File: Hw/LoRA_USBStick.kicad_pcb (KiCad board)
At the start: 2 copper layers, 61.5 x 18.7 mm, 18 parts, among them J10 USB_B, J4 SWD, SW1 RST, U1 ATSAMD21E, U2 RFM95W-868S2, U3 AP2112K-3.3

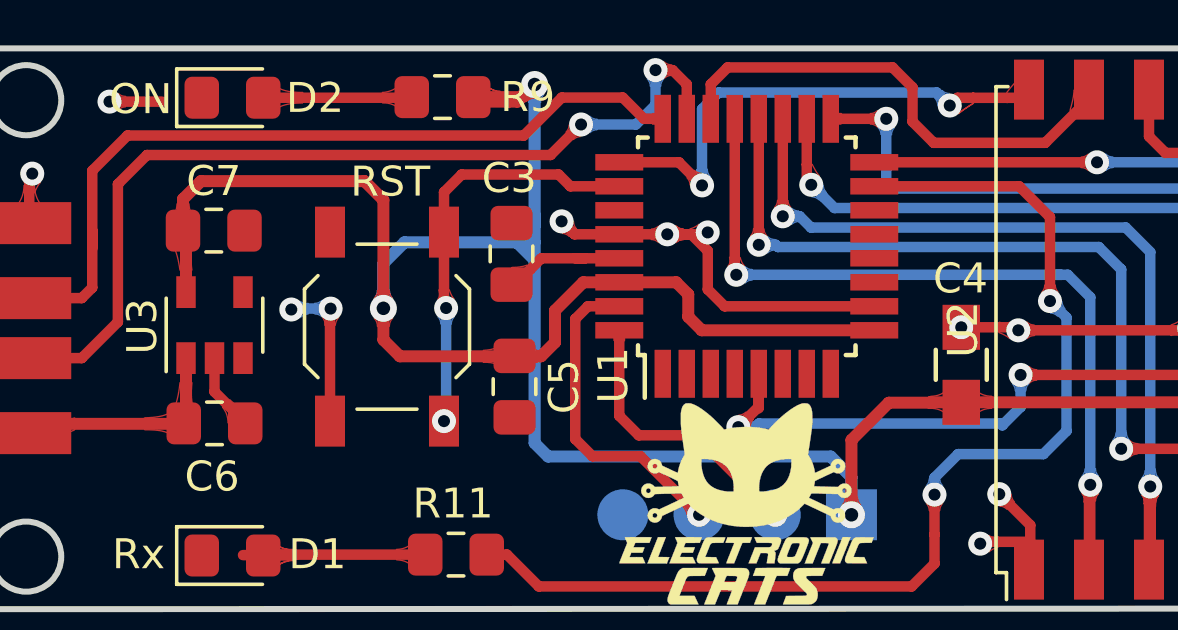
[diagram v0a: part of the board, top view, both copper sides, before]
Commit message: Fix layout on enable LDO
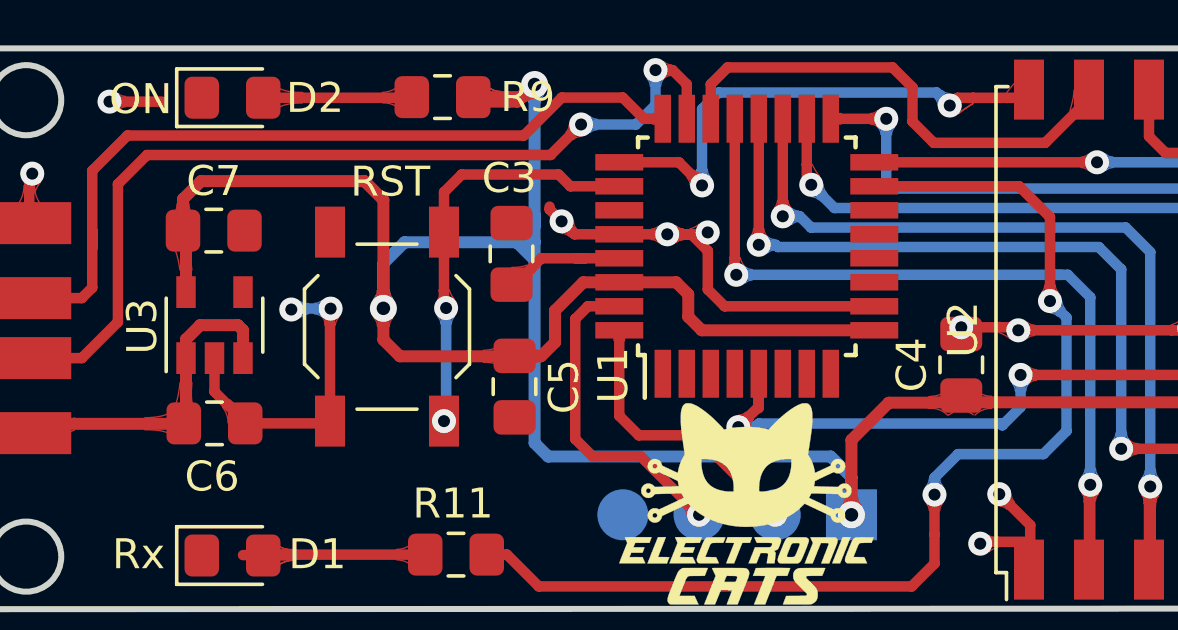
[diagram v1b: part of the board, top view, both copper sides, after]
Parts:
- C4: footprint Capacitors_SMD:C_0805_HandSoldering -> Capacitor_SMD:C_0805_2012Metric_Pad1.15x1.40mm_HandSolder
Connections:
- U3 pad 3: Net-(U3-Pad3) -> VBUS
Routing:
- net VBUS: track 6.92 -> 10.6 mm
- net GND: track 57.1 -> 60.6 mm

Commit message: Change labels, assigned and check the footprints
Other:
- net class Default removed
- net class Vcc+ removed
- net class vcc removed

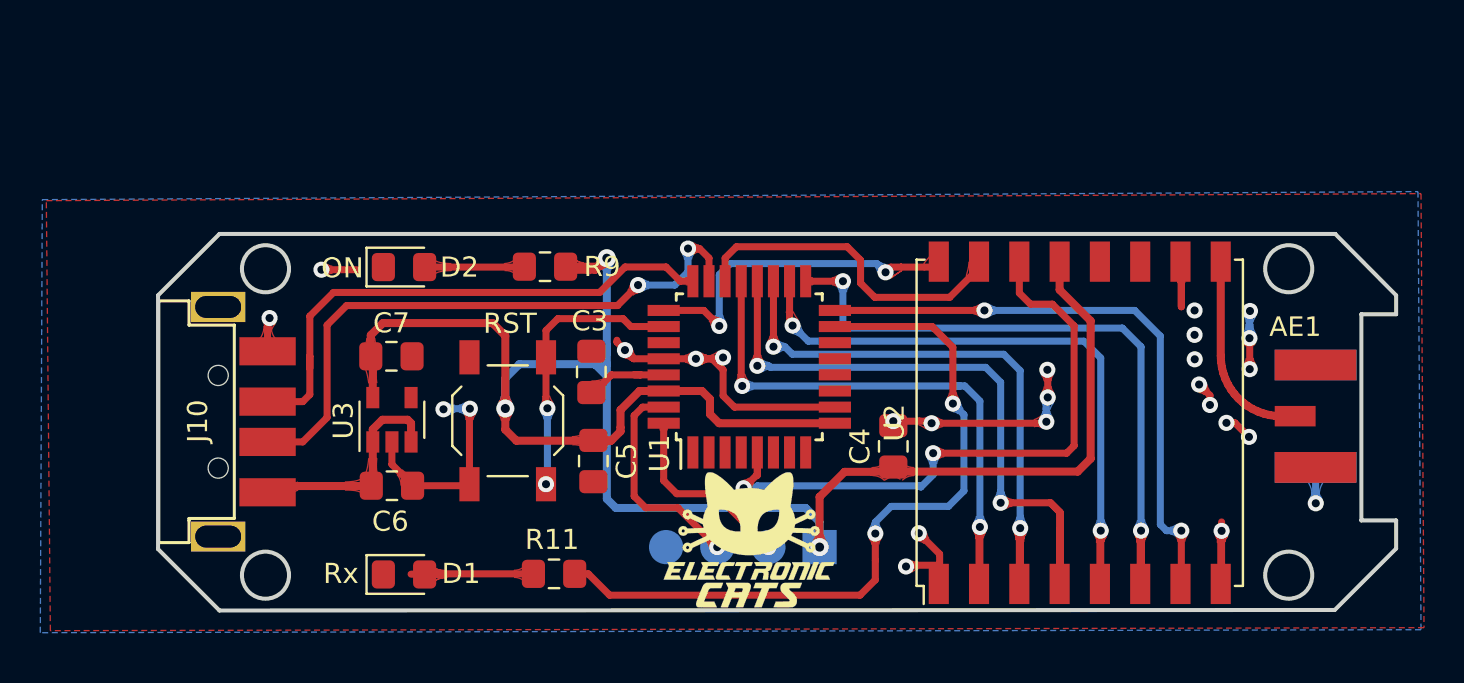
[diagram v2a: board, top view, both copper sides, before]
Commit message: Place footprints on the PCB
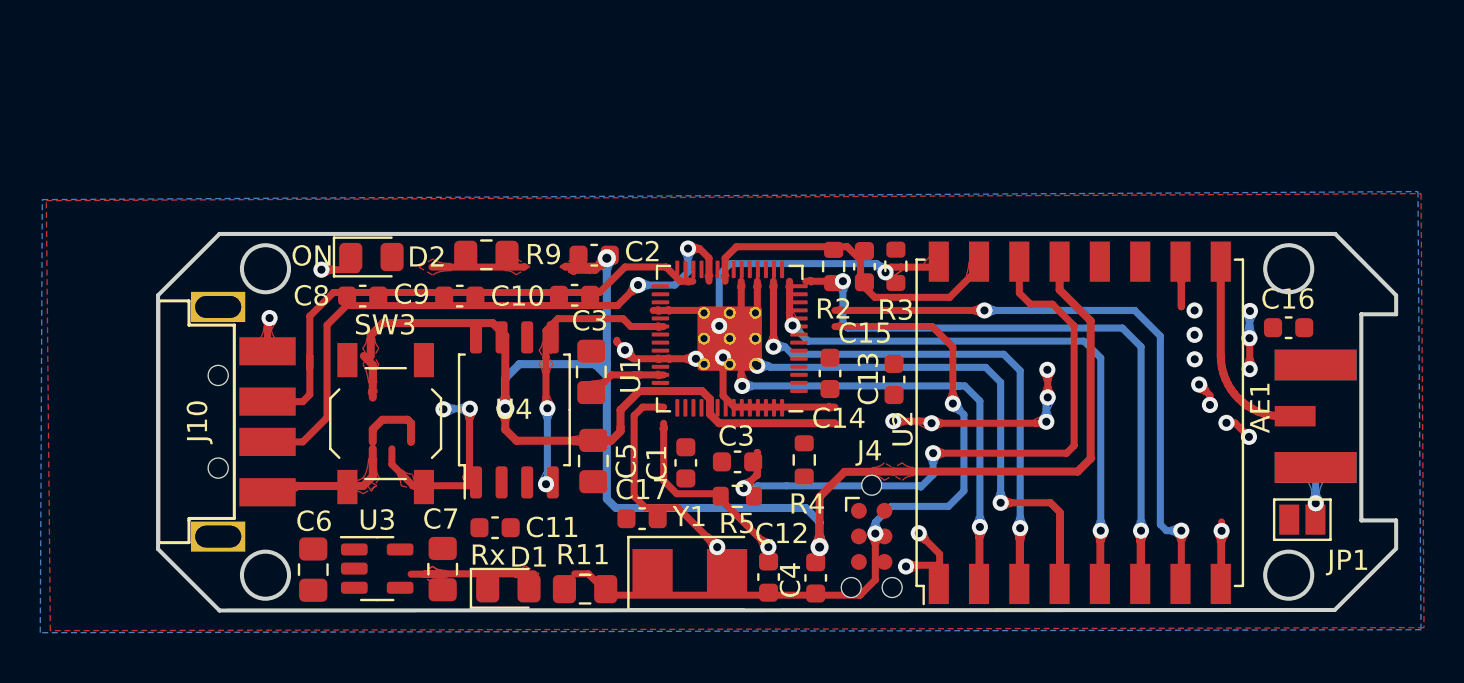
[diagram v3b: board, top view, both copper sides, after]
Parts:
- removed the G*** at (146.1, 120.0)
- removed SW1: RST, Button_Switch_SMD:SW_SPST_TL3342
- added C1: 27pF, Capacitor_SMD:C_0603_1608Metric, F.Cu at (143.0, 116.1)
- added C10: 0.1uF, Capacitor_SMD:C_0603_1608Metric, F.Cu at (137.5, 107.8)
- added C11: 0.1uF, Capacitor_SMD:C_0603_1608Metric, F.Cu at (133.5, 119.4)
- added C12: 0.1uF, Capacitor_SMD:C_0603_1608Metric, F.Cu at (147.1, 121.8)
- added C13: 0.1uF, Capacitor_SMD:C_0603_1608Metric, F.Cu at (153.3, 112.0)
- added C14: 0.1uF, Capacitor_SMD:C_0603_1608Metric, F.Cu at (150.2, 111.7)
- added C15: 0.1uF, Capacitor_SMD:C_0603_1608Metric, F.Cu at (151.9, 106.4)
- added C16: 0.1uF, Capacitor_SMD:C_0603_1608Metric, F.Cu at (172.9, 109.4)
- added C17: 0.1uF, Capacitor_SMD:C_0603_1608Metric, F.Cu at (140.8, 118.9)
- added C2: 1uF, Capacitor_SMD:C_0603_1608Metric, F.Cu at (138.4, 105.8)
- added C3: 27pF, Capacitor_SMD:C_0603_1608Metric, F.Cu at (145.6, 116.1)
- added C8: 0.1uF, Capacitor_SMD:C_0603_1608Metric, F.Cu at (127.0, 107.9)
- added C9: 1uF, Capacitor_SMD:C_0603_1608Metric, F.Cu at (131.8, 107.9)
- added JP1: BOOT, Jumper:SolderJumper-2_P1.3mm_Open_Pad1.0x1.5mm, F.Cu at (173.6, 119.0)
- added R2: 1K, Resistor_SMD:R_0603_1608Metric, F.Cu at (150.3, 106.4)
- added R3: 27, Resistor_SMD:R_0603_1608Metric, F.Cu at (153.4, 106.4)
- added R4: 27, Resistor_SMD:R_0603_1608Metric, F.Cu at (148.9, 116.0)
- added R5: 10K, Resistor_SMD:R_0603_1608Metric, F.Cu at (145.6, 117.8)
- added SW3: RST, Button_Switch_SMD:SW_SPST_TL3342, F.Cu at (128.1, 114.2)
- added U4: W25Q16JV, Package_SO:SOIC-8_5.275x5.275mm_P1.27mm, F.Cu at (134.5, 113.5)
- added Y1: 12Mhz, Crystal:Crystal_SMD_5032-2Pin_5.0x3.2mm, F.Cu at (143.2, 121.6)
- C4: footprint Capacitor_SMD:C_0805_2012Metric_Pad1.15x1.40mm_HandSolder -> Capacitor_SMD:C_0603_1608Metric
- J4: footprint Pin_Headers:Pin_Header_Straight_1x04_Pitch2.54mm -> Connector:Tag-Connect_TC2030-IDC-NL_2x03_P1.27mm_Vertical; moved to F.Cu
- U1: value ATSAMD21E -> RP2040; footprint Housings_QFP:TQFP-32_7x7mm_Pitch0.8mm -> RP2040:RP2040-QFN-56
- moved C7 10.9 mm to (130.9, 121.4), turned to -90 degrees
- moved C4 7.58 mm to (149.4, 121.8), turned to -90 degrees
- moved U3 7.43 mm to (127.7, 121.4), turned to 0 degrees
- moved C6 5.71 mm to (124.5, 121.4), turned to -90 degrees
- moved D1 5.23 mm to (134.2, 122.4)
- moved R9 2.97 mm to (133.1, 105.8)
- moved J4 2.64 mm to (152.2, 119.8), turned to -90 degrees
- moved R11 1.72 mm to (138.0, 122.4)
- moved U1 1.71 mm to (145.2, 110.0), turned to 180 degrees
- moved D2 1.69 mm to (127.4, 105.9)
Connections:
- net Net-(U1-Pad2) renamed /RX_LED
- C4 pad 1: +3V3 -> +1V2
- J4 pad 3: /SWCLK -> /RST
- J4 pad 4: GND -> /SWCLK
- U1 pad 1: Net-(U1-Pad1) -> +3V3
- U1 pad 10: GND -> +3V3
- U1 pad 11: Net-(U1-Pad11) -> unconnected-(U1-Pad11)
- U1 pad 12: Net-(U1-Pad12) -> unconnected-(U1-Pad12)
- U1 pad 13: Net-(U1-Pad13) -> /DIO0
- U1 pad 14: Net-(U1-Pad14) -> /DIO1
- U1 pad 15: /Rx_LED -> /DIO2
- U1 pad 16: /DIO5 -> unconnected-(U1-Pad16)
- U1 pad 17: /RFM_RST -> unconnected-(U1-Pad17)
- U1 pad 18: /SS -> /DIO5
- U1 pad 19: /MOSI -> GND
- U1 pad 20: /SCK -> Net-(C1-Pad1)
- U1 pad 21: /MISO -> Net-(R2-Pad2)
- U1 pad 22: /DIO1 -> +3V3
- U1 pad 23: /D- -> +1V2
- U1 pad 24: /D+ -> /SWCLK
- U1 pad 25: /DIO2 -> /SWDIO
- U1 pad 27: Net-(U1-Pad27) -> /MISO
- U1 pad 28: GND -> /SS
- U1 pad 29: Net-(C3-Pad1) -> /SCK
- U1 pad 3: Net-(U1-Pad3) -> unconnected-(U1-Pad3)
- U1 pad 30: +3V3 -> /MOSI
- U1 pad 31: /SWCLK -> unconnected-(U1-Pad31)
- U1 pad 32: /SWDIO -> /RFM_RST
- U1 pad 4: Net-(U1-Pad4) -> unconnected-(U1-Pad4)
- U1 pad 5: /DIO0 -> unconnected-(U1-Pad5)
- U1 pad 6: Net-(U1-Pad6) -> unconnected-(U1-Pad6)
- U1 pad 7: Net-(U1-Pad7) -> unconnected-(U1-Pad7)
- U1 pad 8: Net-(U1-Pad8) -> unconnected-(U1-Pad8)
- U1 pad 9: +3V3 -> unconnected-(U1-Pad9)
- U2 pad 11: Net-(U2-Pad11) -> unconnected-(U2-Pad11)
- U2 pad 12: Net-(U2-Pad12) -> unconnected-(U2-Pad12)
- U3 pad 4: Net-(U3-Pad4) -> unconnected-(U3-Pad4)
- U3 pad 5: +3V3 -> unconnected-(U3-Pad5)
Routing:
- net GND: track 60.6 -> 248.2 mm, vias 26 -> 31
- net /Rx_LED: track 37.2 -> 0.00 mm, vias 2 -> 0
- net /SS: track 31.4 -> 66.0 mm, vias 2 -> 4
- net /RFM_RST: track 34.6 -> 0.00 mm, vias 2 -> 0
- net /SCK: track 34.5 -> 0.00 mm, vias 2 -> 0
- net Net-(C3-Pad1): track 4.50 -> 36.6 mm, vias 0 -> 2
- net /DIO0: track 32.1 -> 0.00 mm, vias 2 -> 0
- net unconnected-(U1-Pad16): track 0.00 -> 30.5 mm, vias 0 -> 2
- net /MOSI: track 30.5 -> 0.00 mm, vias 2 -> 0
- net /MISO: track 28.6 -> 0.00 mm, vias 2 -> 0
- net /D+: track 28.3 -> 0.00 mm
- net /QSPI_CS: track 0.00 -> 21.4 mm, vias 0 -> 4
- net +3V3: track 98.9 -> 119.8 mm
- net /D-: track 30.8 -> 10.3 mm, vias 2 -> 5
- net /DIO2: track 17.6 -> 0.00 mm, vias 2 -> 0
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
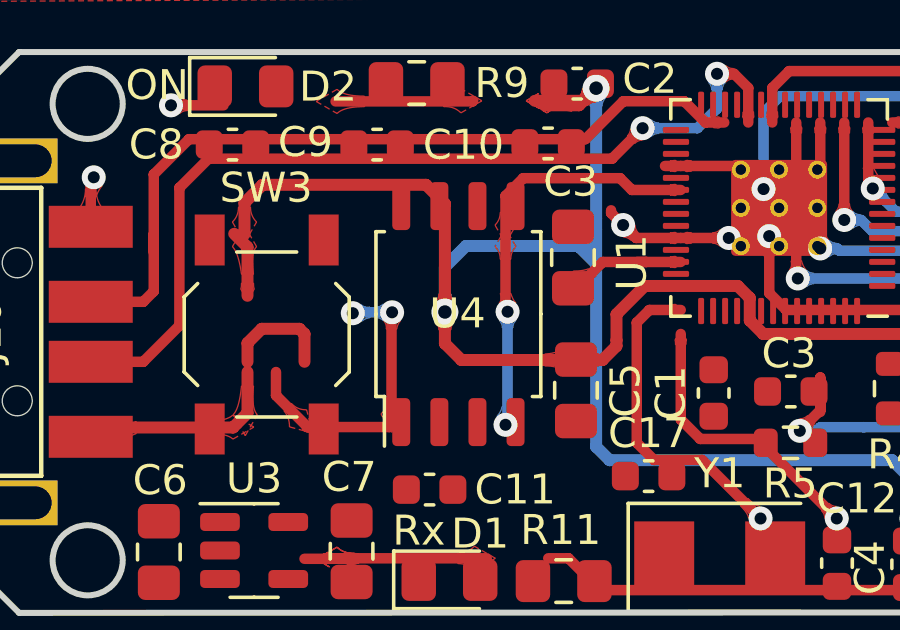
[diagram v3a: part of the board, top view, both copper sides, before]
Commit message: add footprint memory flash
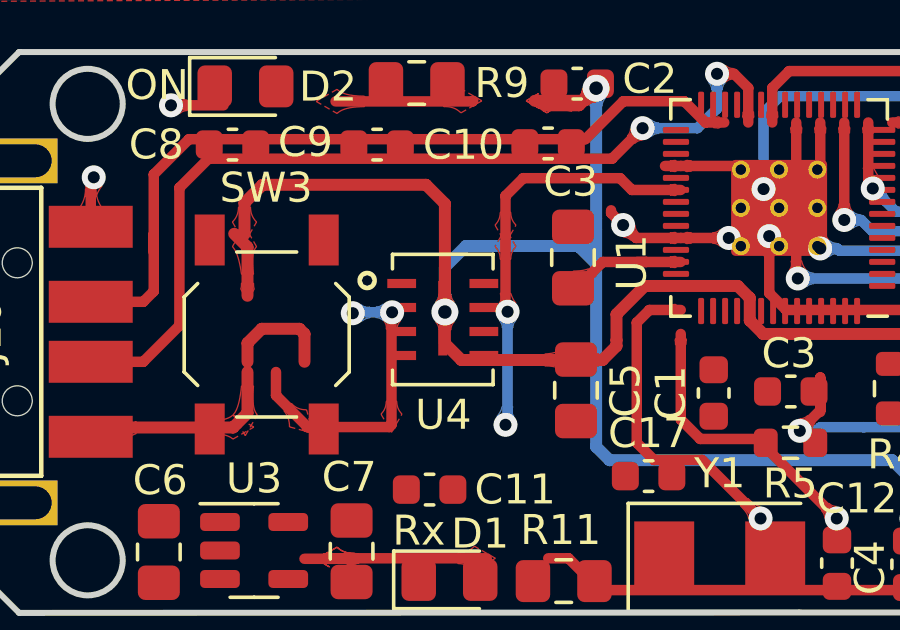
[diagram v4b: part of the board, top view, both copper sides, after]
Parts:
- U4: footprint Package_SO:SOIC-8_5.275x5.275mm_P1.27mm -> RP2040:W25Q16JVUUIQ
- moved U4 0.55 mm to (134.0, 113.7), turned to 0 degrees
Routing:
- net /SS: track 66.0 -> 0.00 mm, vias 4 -> 0
- net Net-(C3-Pad1): track 36.6 -> 70.5 mm, vias 2 -> 4
- net +3V3: track 119.8 -> 151.9 mm, vias 3 -> 5
- net unconnected-(U1-Pad16): track 30.5 -> 0.00 mm, vias 2 -> 0
- net /MOSI: track 0.00 -> 30.5 mm, vias 0 -> 2
- net unconnected-(U1-Pad34): track 0.00 -> 13.9 mm, vias 0 -> 2
- net VBUS: track 0.00 -> 10.6 mm
- net /RST: track 10.6 -> 0.00 mm
- net /QSPI_CS: track 21.4 -> 11.2 mm, vias 4 -> 2
- net GND: track 248.2 -> 244.5 mm

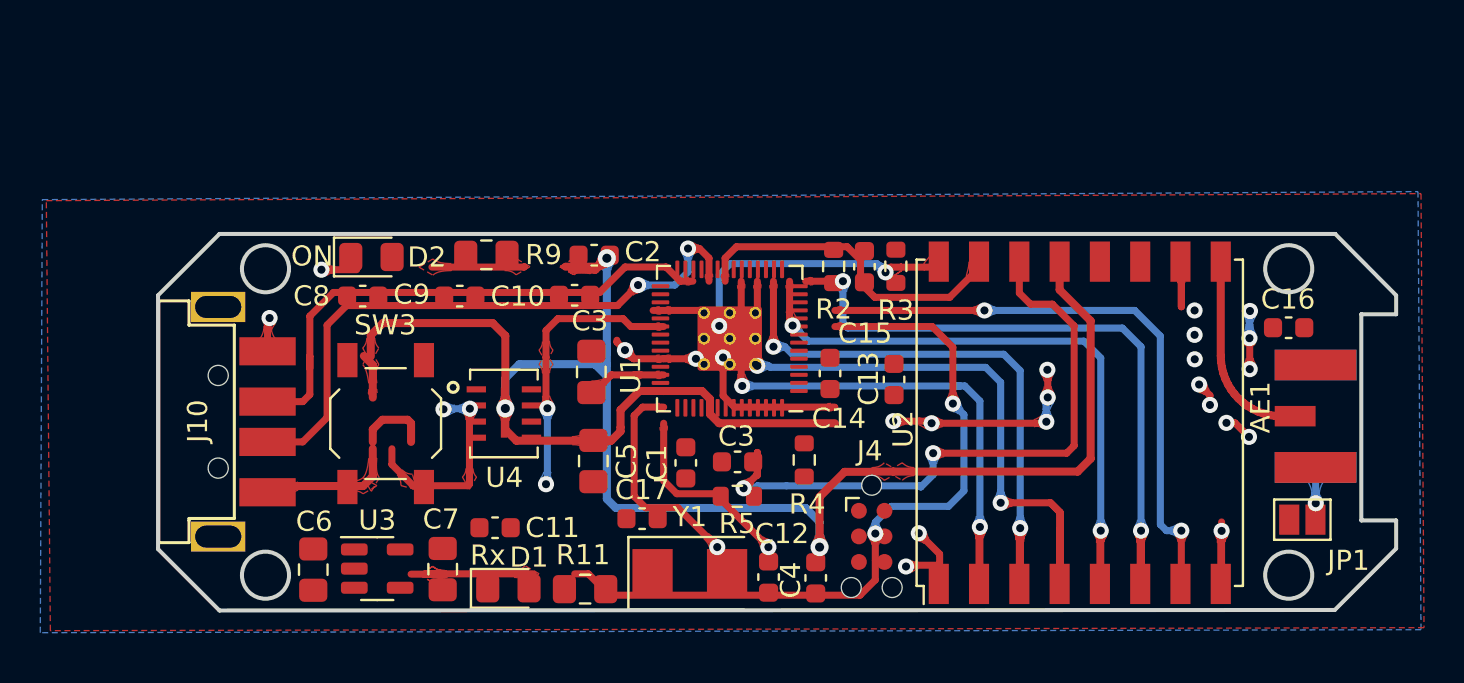
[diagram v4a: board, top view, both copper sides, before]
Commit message: New floor plan
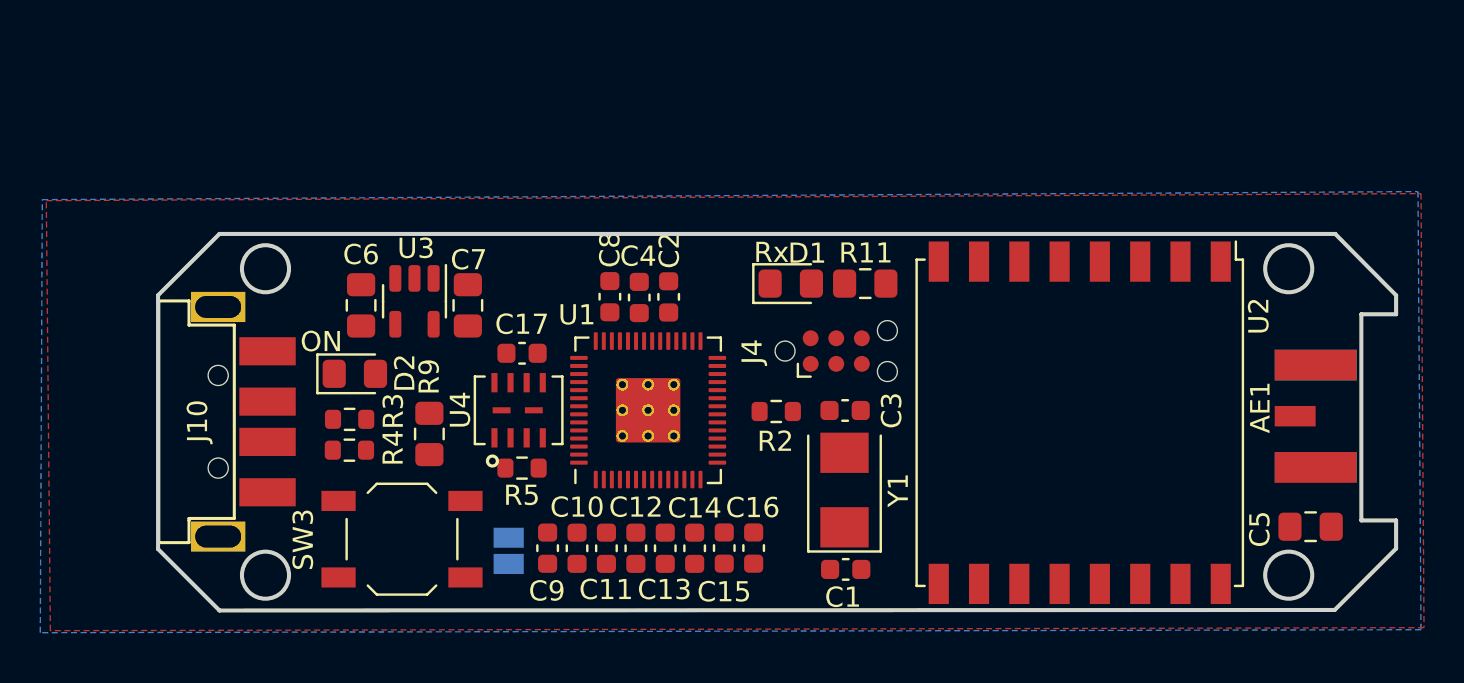
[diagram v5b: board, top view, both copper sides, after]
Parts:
- removed the C3 at (138.3, 111.6)
- JP1: moved to B.Cu
- moved JP1 39.4 mm to (134.2, 120.5), turned to 90 degrees
- moved C5 35.8 mm to (174.0, 119.3), turned to 0 degrees
- moved C16 28.7 mm to (146.4, 120.4), turned to -90 degrees
- moved R3 28.2 mm to (126.3, 114.0), turned to 0 degrees
- moved R4 22.6 mm to (126.3, 115.5), turned to 0 degrees
- moved D1 20.6 mm to (148.2, 107.2)
- moved R11 20.6 mm to (151.9, 107.2)
- moved C4 16.4 mm to (140.7, 107.9), turned to 90 degrees
- moved C15 15.6 mm to (144.9, 120.4), turned to -90 degrees
- moved C13 14.1 mm to (142.0, 120.4), turned to -90 degrees
- moved U3 13.4 mm to (129.5, 108.1), turned to -90 degrees
- moved C6 13.3 mm to (126.9, 108.3)
- moved C9 13.3 mm to (136.1, 120.4), turned to -90 degrees
- moved C7 13.2 mm to (132.2, 108.3)
- moved C10 12.6 mm to (137.6, 120.4), turned to -90 degrees
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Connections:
- U3 pad 5: unconnected-(U3-Pad5) -> +3V3
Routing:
- net GND: track 244.5 -> 0.00 mm, vias 31 -> 0
- net +3V3: track 151.9 -> 0.00 mm, vias 5 -> 0
- net Net-(C3-Pad1): track 70.5 -> 0.00 mm, vias 4 -> 0
- net /MOSI: track 30.5 -> 0.00 mm, vias 2 -> 0
- net /DIO5: track 28.9 -> 0.00 mm, vias 2 -> 0
- net unconnected-(U1-Pad34): track 13.9 -> 0.00 mm, vias 2 -> 0
- net /QSPI_CS: track 11.2 -> 0.00 mm, vias 2 -> 0
- net VBUS: track 10.6 -> 0.00 mm
- net /D-: track 10.3 -> 0.00 mm, vias 5 -> 0
- net Net-(AE1-Pad1): track 10.1 -> 0.00 mm
